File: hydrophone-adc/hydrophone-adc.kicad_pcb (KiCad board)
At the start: 4 copper layers, 152.8 x 66.3 mm, 202 parts, among them J1001 TEST_1P, J1002 TEST_1P, J1003 TEST_1P, J1004 TEST_1P, J1005 TEST_1P, J1006 TEST_1P, J1007 TEST_1P, J1101 TEST_1P, J1102 TEST_1P, J1201 TEST_1P, J1202 TEST_1P, J1203 TEST_1P, J1204 TEST_1P, J1205 TEST_1P, J1206 TEST_1P, J1207 TEST_1P, J1301 BARREL_JACK, J401 CONN_COAXIAL, J402 CONN_COAXIAL, J403 CONN_COAXIAL, J404 CONN_COAXIAL, J501 TEST_1P, J502 TEST_1P, J601 TEST_1P, J602 TEST_1P, J603 TEST_1P, J604 TEST_1P, J605 TEST_1P, J606 TEST_1P, J607 TEST_1P, J701 TEST_1P, J702 TEST_1P, J801 TEST_1P, J802 TEST_1P, J803 TEST_1P, J804 TEST_1P, J805 TEST_1P, J806 TEST_1P, J807 TEST_1P, J901 TEST_1P, J902 TEST_1P, U1001 LM324, U1101 el5170, U1201 LM324, U1301 TS30013, U1302 LM2776, U1303 LT1963, U201 micro-zed-jx1, U301 micro-zed-jx2, U401 LTC2171-14, U501 el5170, U601 LM324, U701 el5170, U801 LM324, U901 el5170

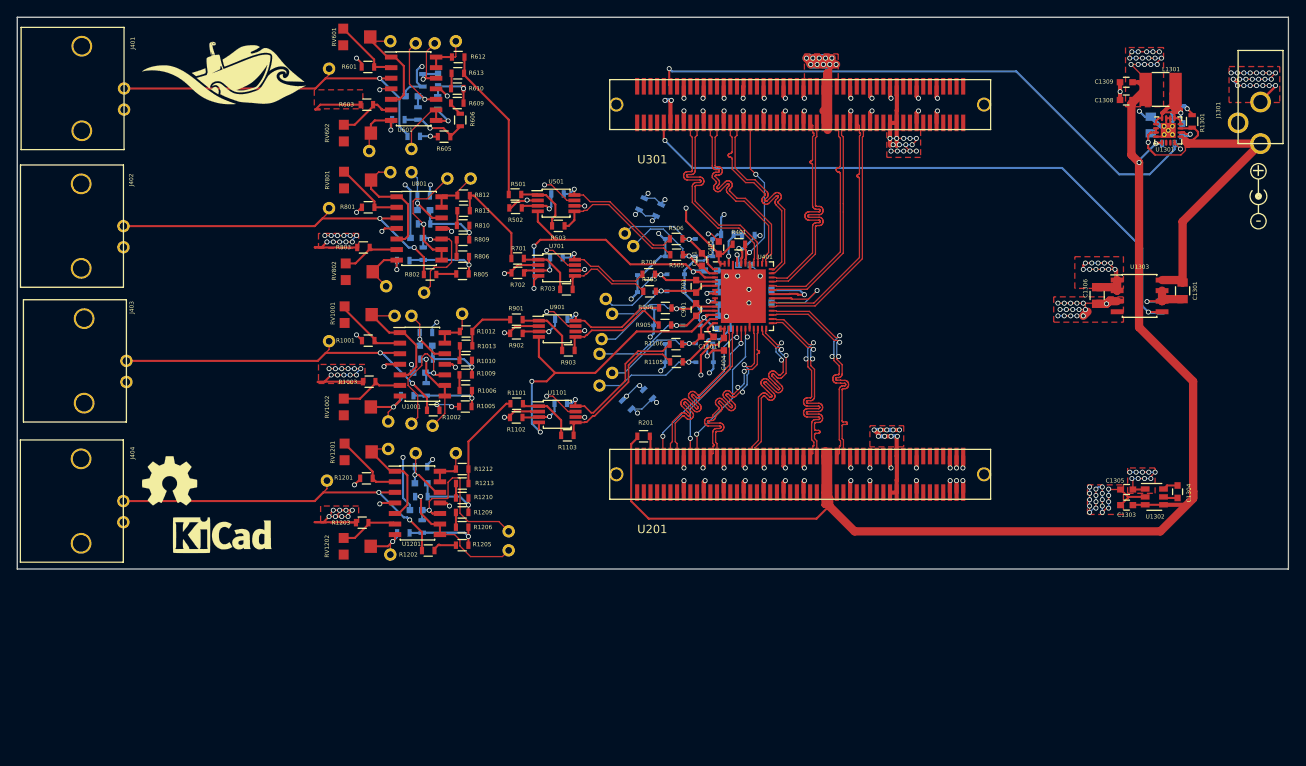
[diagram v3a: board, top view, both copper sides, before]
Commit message: Updated hydrophone board post review
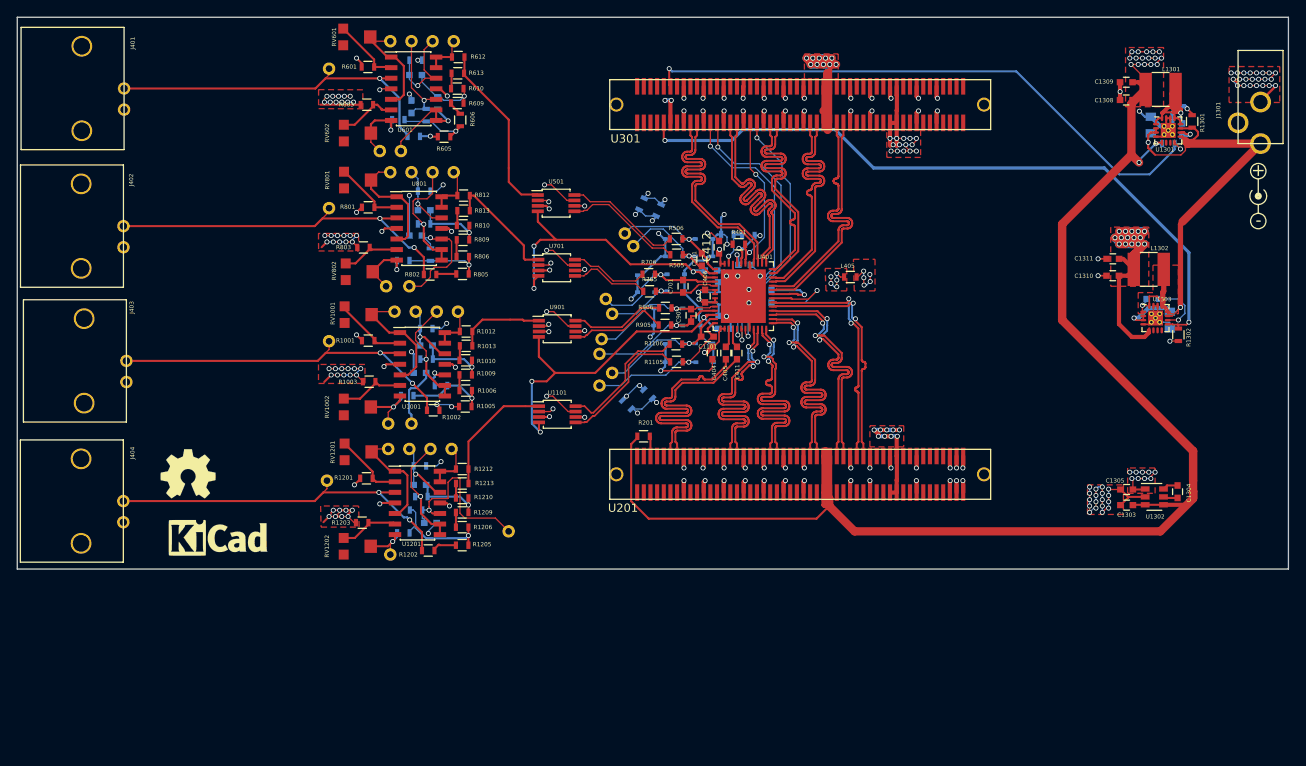
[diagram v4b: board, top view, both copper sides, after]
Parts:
- removed G***: LOGO, robosub_footprints:robosub_logo-large
- removed R1101, R1102, R1103, R1104, R501, R502, R503, R504, R701, R702, R703, R704, R901, R902, R903, R904: 10k .1%, Resistors_SMD:R_0603
- added C1310: 22u, Capacitors_SMD:C_0603, F.Cu at (215.4, 71.4)
- added C1311: 22u, Capacitors_SMD:C_0603, F.Cu at (215.4, 69.3)
- added C411: 100n, Capacitors_SMD:C_0603, F.Cu at (170.2, 80.7)
- added C412: 1u, Capacitors_SMD:C_0603, F.Cu at (168.1, 67.9)
- added L1302: 4.7u, robosub_footprints:Inductor-3.6mm-Pitch-4.0mm-Length-1.5mm-Width, F.Cu at (219.7, 70.6)
- added L405: Ferrite_Bead, Resistors_SMD:R_0603, F.Cu at (183.8, 71.5)
- C1301: moved to B.Cu
- C1306: value 10u -> 22n; footprint Capacitors_SMD:C_0805 -> Capacitors_SMD:C_0603; moved to B.Cu
- C406: moved to F.Cu
- R1302: value 100k -> 10k; moved to F.Cu
- U1303: value LT1963 -> TS30042; footprint Housings_SOIC:SOIC-8_3.9x4.9mm_Pitch1.27mm -> Housings_DFN_QFN:QFN-16-1EP_3x3mm_Pitch0.5mm_ThermalVias
- moved J1205 15.4 mm to (133.3, 92.2)
- moved J1005 13.7 mm to (134.1, 75.7)
- moved C405 12.7 mm to (168.9, 80.7)
- moved R807 7.51 mm to (132.6, 61.2), turned to 0 degrees
- moved R1007 7.32 mm to (132.8, 77.7), turned to 0 degrees
- moved R1207 7.29 mm to (132.1, 94.2), turned to 0 degrees
- moved R811 7.10 mm to (133.3, 68.8), turned to 270 degrees
- moved C1306 6.73 mm to (220.2, 74.2), turned to 0 degrees
- moved R1011 6.64 mm to (134.6, 84.6)
- moved R607 6.40 mm to (131.6, 45.5), turned to 0 degrees
- moved R1211 5.25 mm to (131.6, 99.5), turned to 180 degrees
- moved C1202 4.89 mm to (133.3, 101.1), turned to 180 degrees
- moved C602 4.52 mm to (131.1, 51.1)
- moved R611 4.20 mm to (132.8, 52.1)
- moved R1302 4.00 mm to (223.3, 78.5), turned to 270 degrees
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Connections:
- C1001 pad 2: GNDREF -> Net-(C1001-Pad2)
- C1002 pad 1: Net-(C1002-Pad1) -> GNDREF
- C1201 pad 2: GNDREF -> Net-(C1201-Pad2)
- C1202 pad 1: Net-(C1202-Pad1) -> GNDREF
- C1306 pad 1: +1V8 -> Net-(C1306-Pad1)
- C1306 pad 2: GND -> Net-(C1306-Pad2)
- C404 pad 1: +1V8 -> /ADC/1v8_analog
- C405 pad 1: +1V8 -> /samp_clk+
- C405 pad 2: GNDREF -> /ADC/enc+
- C601 pad 2: GNDREF -> Net-(C601-Pad2)
- C602 pad 1: Net-(C602-Pad1) -> GNDREF
- C801 pad 2: GNDREF -> Net-(C801-Pad2)
- C802 pad 1: Net-(C802-Pad1) -> GNDREF
- J1004 pad 1: Net-(C1001-Pad1) -> Net-(C1002-Pad2)
- J1006 pad 1: Net-(C1002-Pad1) -> Net-(C1001-Pad1)
- J1204 pad 1: Net-(C1201-Pad1) -> Net-(C1202-Pad2)
- J1206 pad 1: Net-(C1202-Pad1) -> Net-(C1201-Pad1)
- J604 pad 1: Net-(C601-Pad1) -> Net-(C602-Pad2)
- J606 pad 1: Net-(C602-Pad1) -> Net-(C601-Pad1)
- J804 pad 1: Net-(C801-Pad1) -> Net-(C802-Pad2)
- J806 pad 1: Net-(C802-Pad1) -> Net-(C801-Pad1)
- R1007 pad 1: Net-(R1004-Pad1) -> Net-(C1001-Pad1)
- R1007 pad 2: Net-(C1001-Pad1) -> GNDREF
- R1008 pad 1: Net-(C1002-Pad2) -> Net-(C1001-Pad2)
- R1009 pad 1: Net-(C1002-Pad2) -> Net-(C1001-Pad2)
- R1010 pad 1: Net-(C1002-Pad2) -> Net-(C1001-Pad2)
- R1011 pad 1: Net-(C1002-Pad1) -> Net-(C1002-Pad2)
- R1011 pad 2: GNDREF -> Net-(R1004-Pad1)
- R1105 pad 1: /ADC/Diff Conv4/v+ -> /ADC/Diff Conv4/v-
- R1106 pad 1: /ADC/Diff Conv4/v- -> /ADC/Diff Conv4/v+
- R1207 pad 1: Net-(R1204-Pad1) -> Net-(C1201-Pad1)
- R1207 pad 2: Net-(C1201-Pad1) -> GNDREF
- R1208 pad 1: Net-(C1202-Pad2) -> Net-(C1201-Pad2)
- R1209 pad 1: Net-(C1202-Pad2) -> Net-(C1201-Pad2)
- R1210 pad 1: Net-(C1202-Pad2) -> Net-(C1201-Pad2)
- R1211 pad 1: Net-(C1202-Pad1) -> Net-(C1202-Pad2)
- R1211 pad 2: GNDREF -> Net-(R1204-Pad1)
- R505 pad 1: /ADC/Diff Conv1/v+ -> /ADC/Diff Conv1/v-
- R506 pad 1: /ADC/Diff Conv1/v- -> /ADC/Diff Conv1/v+
- R607 pad 1: Net-(R604-Pad1) -> Net-(C601-Pad1)
- R607 pad 2: Net-(C601-Pad1) -> GNDREF
- R608 pad 1: Net-(C602-Pad2) -> Net-(C601-Pad2)
- R609 pad 1: Net-(C602-Pad2) -> Net-(C601-Pad2)
- R610 pad 1: Net-(C602-Pad2) -> Net-(C601-Pad2)
- R611 pad 1: Net-(C602-Pad1) -> Net-(C602-Pad2)
- R611 pad 2: GNDREF -> Net-(R604-Pad1)
- R705 pad 1: /ADC/Diff Conv2/v+ -> /ADC/Diff Conv2/v-
- R706 pad 1: /ADC/Diff Conv2/v- -> /ADC/Diff Conv2/v+
- R807 pad 1: Net-(R804-Pad1) -> Net-(C801-Pad1)
- R807 pad 2: Net-(C801-Pad1) -> GNDREF
- R808 pad 1: Net-(C802-Pad2) -> Net-(C801-Pad2)
- R809 pad 1: Net-(C802-Pad2) -> Net-(C801-Pad2)
- R810 pad 1: Net-(C802-Pad2) -> Net-(C801-Pad2)
- R811 pad 1: Net-(C802-Pad1) -> Net-(C802-Pad2)
- R811 pad 2: GNDREF -> Net-(R804-Pad1)
- R905 pad 1: /ADC/Diff Conv3/v+ -> /ADC/Diff Conv3/v-
- R906 pad 1: /ADC/Diff Conv3/v- -> /ADC/Diff Conv3/v+
- U1001 pad 10: Net-(C1001-Pad1) -> Net-(C1002-Pad2)
- U1001 pad 12: Net-(C1002-Pad1) -> Net-(C1001-Pad1)
- U1101 pad 1: Net-(R1101-Pad1) -> /ADC/Diff Conv4/Vin
- U1101 pad 3: Net-(R1102-Pad1) -> GNDREF
- U1101 pad 5: /ADC/Diff Conv4/v+ -> /ADC/Diff Conv4/v-
- U1101 pad 8: /ADC/Diff Conv4/v- -> /ADC/Diff Conv4/v+
- U1201 pad 10: Net-(C1201-Pad1) -> Net-(C1202-Pad2)
- U1201 pad 12: Net-(C1202-Pad1) -> Net-(C1201-Pad1)
- U1303 pad 1: +1V8 -> Net-(C1306-Pad1)
- U1303 pad 2: +1V8 -> /Power/Vin
- U1303 pad 3: GND -> /Power/Vin
- U1303 pad 4: (no net) -> GND
- U1303 pad 5: /vccio_en -> +1V8
- U1303 pad 6: GND -> (no net)
- U1303 pad 7: GND -> (no net)
- U1303 pad 8: /Power/Vin -> Net-(U1303-Pad8)
- U201 pad 10: /MicroZed-JX1/SE1 -> /MicroZed-JX1/SE0
- U201 pad 17: /SCK -> /MicroZed-JX1/LVDS2+
- U201 pad 19: /MOSI -> /MicroZed-JX1/LVDS2-
- U201 pad 23: /out4b+ -> /MicroZed-JX1/LVDS4+
- U201 pad 25: /out4b- -> /MicroZed-JX1/LVDS4-
- U201 pad 29: /MicroZed-JX1/LVDS6+ -> /out4b+
- U201 pad 31: /MicroZed-JX1/LVDS6- -> /out4b-
- U201 pad 35: /out4a+ -> /MicroZed-JX1/LVDS8+
- U201 pad 37: /out4a- -> /MicroZed-JX1/LVDS8-
- U201 pad 41: /MicroZed-JX1/LVDS10+ -> /out4a+
- U201 pad 43: /MicroZed-JX1/LVDS10- -> /out4a-
- U201 pad 67: /MicroZed-JX1/LVDS18+ -> /fr_clk+
- U201 pad 69: /MicroZed-JX1/LVDS18- -> /fr_clk-
- U201 pad 9: /~CS -> /MicroZed-JX1/SE1
- U301 pad 24: /out1b+ -> /~CS
- U301 pad 26: /out1b- -> /SCK
- U301 pad 30: /out2a+ -> /out1b+
- U301 pad 32: /out2a- -> /out1b-
- U301 pad 38: /MicroZed-JX2/LVDS7- -> /MOSI
- U301 pad 42: /MicroZed-JX2/LVDS9+ -> /out2a+
- U301 pad 44: /MicroZed-JX2/LVDS9- -> /out2a-
- U301 pad 68: /fr_clk+ -> /MicroZed-JX2/LVDS17+
- U301 pad 70: /fr_clk- -> /MicroZed-JX2/LVDS17-
- U401 pad 15: +1V8 -> /ADC/1v8_analog
- U401 pad 16: +1V8 -> /ADC/1v8_analog
- U401 pad 17: /samp_clk+ -> /ADC/enc+
- U401 pad 18: /samp_clk- -> /ADC/enc-
- U401 pad 51: +1V8 -> /ADC/1v8_analog
- U401 pad 52: +1V8 -> /ADC/1v8_analog
- U501 pad 1: Net-(R501-Pad1) -> /ADC/Diff Conv1/Vin
- U501 pad 3: Net-(R502-Pad1) -> GNDREF
- U501 pad 5: /ADC/Diff Conv1/v+ -> /ADC/Diff Conv1/v-
- U501 pad 8: /ADC/Diff Conv1/v- -> /ADC/Diff Conv1/v+
- U601 pad 10: Net-(C601-Pad1) -> Net-(C602-Pad2)
- U601 pad 12: Net-(C602-Pad1) -> Net-(C601-Pad1)
- U701 pad 1: Net-(R701-Pad1) -> /ADC/Diff Conv2/Vin
- U701 pad 3: Net-(R702-Pad1) -> GNDREF
- U701 pad 5: /ADC/Diff Conv2/v+ -> /ADC/Diff Conv2/v-
- U701 pad 8: /ADC/Diff Conv2/v- -> /ADC/Diff Conv2/v+
- U801 pad 10: Net-(C801-Pad1) -> Net-(C802-Pad2)
- U801 pad 12: Net-(C802-Pad1) -> Net-(C801-Pad1)
- U901 pad 1: Net-(R901-Pad1) -> /ADC/Diff Conv3/Vin
- U901 pad 3: Net-(R902-Pad1) -> GNDREF
- U901 pad 5: /ADC/Diff Conv3/v+ -> /ADC/Diff Conv3/v-
- U901 pad 8: /ADC/Diff Conv3/v- -> /ADC/Diff Conv3/v+
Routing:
- net /ADC/1v8_analog: track 0.00 -> 45.7 mm, vias 0 -> 7
- net /vccio_en: track 76.3 -> 96.9 mm
- net Net-(C1306-Pad1): track 0.00 -> 18.1 mm, vias 0 -> 1
- net /SCK: track 17.9 -> 34.4 mm
- net GND: track 190.0 -> 173.7 mm, vias 117 -> 103
- net /~CS: track 19.3 -> 33.0 mm
- net Net-(C1202-Pad2): track 8.67 -> 22.1 mm
- net Net-(C1201-Pad1): track 21.5 -> 8.55 mm
- net /MOSI: track 18.0 -> 30.4 mm
- net /Power/Vin: track 48.5 -> 59.2 mm, vias 1 -> 3
- net Net-(C602-Pad1): track 8.95 -> 0.00 mm, vias 1 -> 0
- net Net-(C601-Pad2): track 0.00 -> 8.93 mm, vias 0 -> 1
- net Net-(C1201-Pad2): track 0.00 -> 8.55 mm, vias 0 -> 1
- net Net-(C1202-Pad1): track 8.55 -> 0.00 mm, vias 1 -> 0
- net Net-(C1002-Pad1): track 8.54 -> 0.00 mm, vias 1 -> 0
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- added copper zone on F.Cu, net /ADC/1v8_analog
- added copper zone on F.Cu, net Net-(C1306-Pad1)
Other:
- net class Default: clearance 0.1524 -> 0.127
- rule trace_clearance: 0.1524 -> 0.127

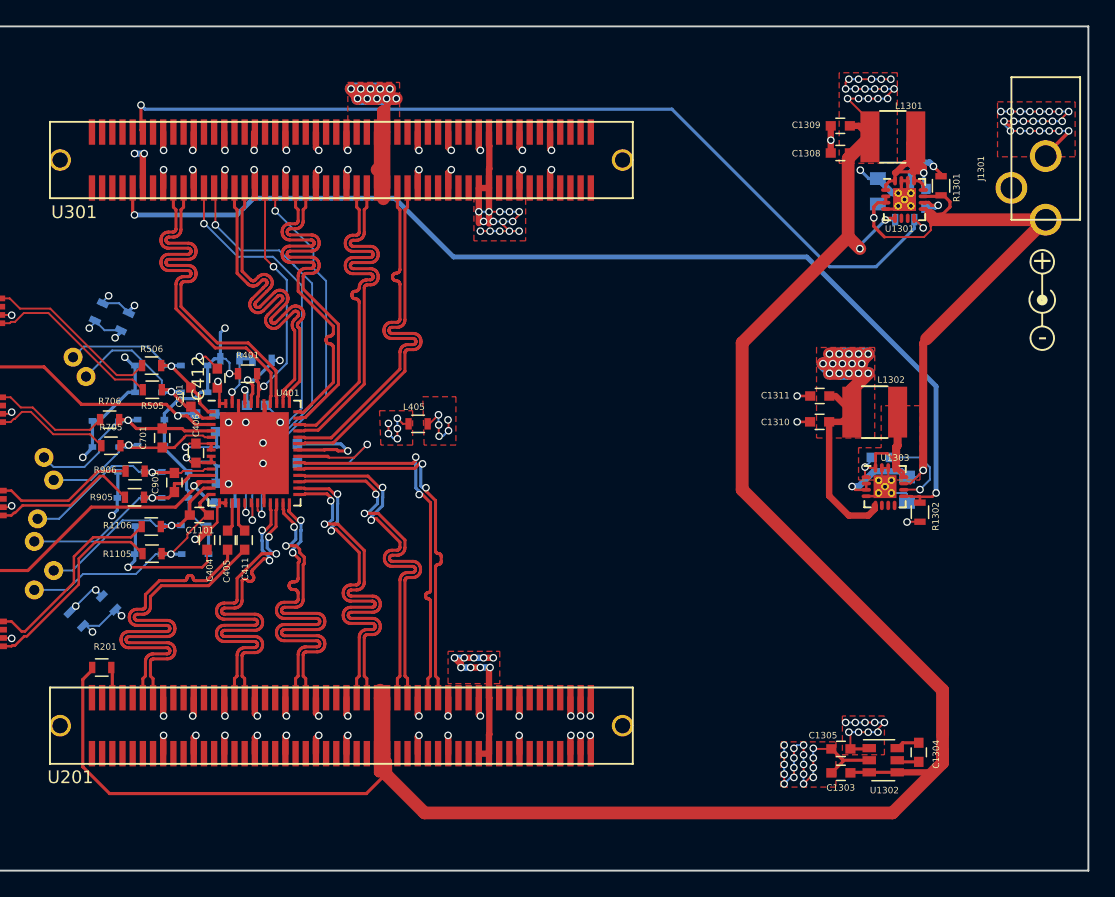
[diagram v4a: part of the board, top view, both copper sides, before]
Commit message: Added LEDs to board and schematic
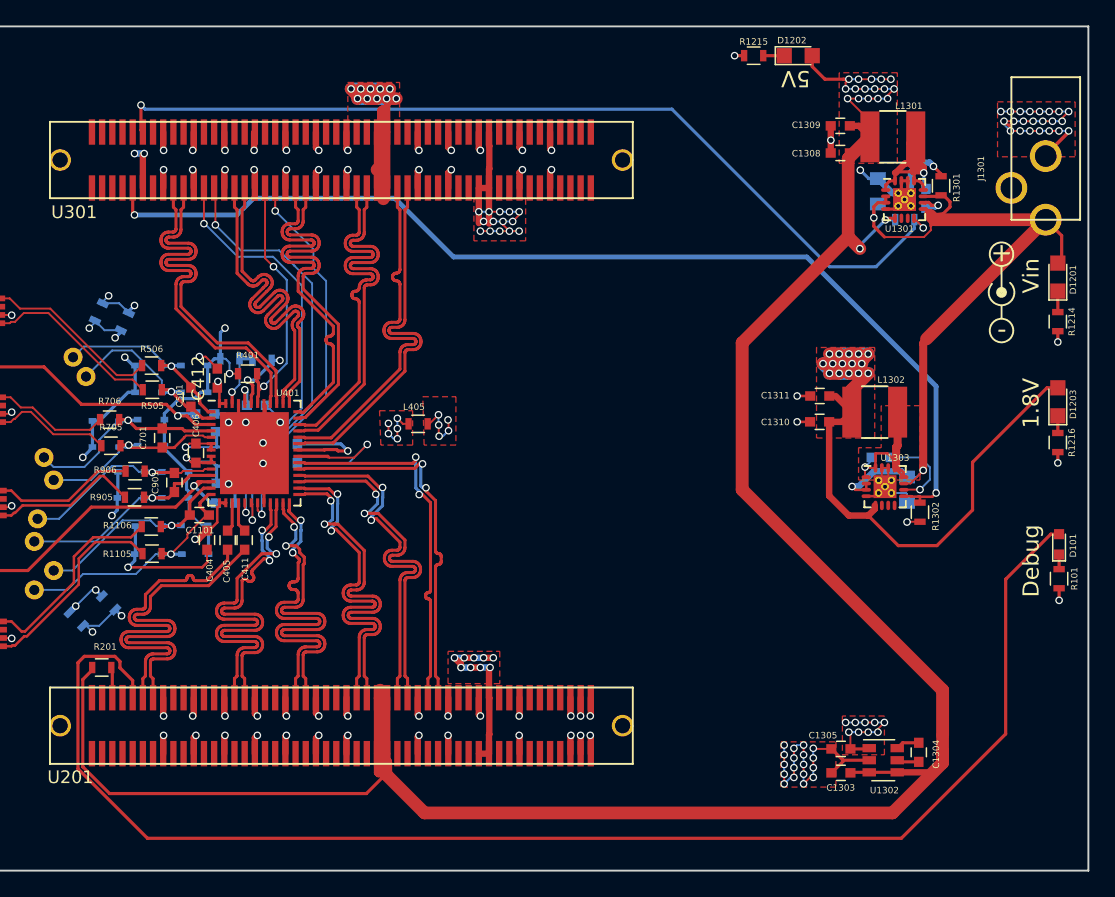
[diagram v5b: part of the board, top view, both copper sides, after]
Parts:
- added D101: ORG, LEDs:LED_0603, F.Cu at (234.2, 81.0)
- added D1201: YLW, LEDs:LED_0805, F.Cu at (234.1, 60.0)
- added D1202: RED, LEDs:LED_0805, F.Cu at (213.7, 42.6)
- added D1203: GRN, LEDs:LED_0805, F.Cu at (234.1, 69.8)
- added R101: 1k, Resistors_SMD:R_0603, F.Cu at (234.2, 83.7)
- added R1214: 1k, Resistors_SMD:R_0603, F.Cu at (234.1, 63.5)
- added R1215: 1k, Resistors_SMD:R_0603, F.Cu at (210.2, 42.6)
- added R1216: 1k, Resistors_SMD:R_0603, F.Cu at (234.1, 73.0)
- moved REF** 3.26 mm to (229.6, 61.2)
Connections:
- net /samp_clk+ renamed /enc+
- net /samp_clk- renamed /enc-
- R401 pad 2: /MISO -> /MOSI
- U201 pad 10: /MicroZed-JX1/SE0 -> /MicroZed-JX1/SE1
- U201 pad 9: /MicroZed-JX1/SE1 -> /MicroZed-JX1/SE0
- U301 pad 36: /MISO -> /MOSI
- U301 pad 38: /MOSI -> /MISO
- U401 pad 21: /MOSI -> /MISO
- U401 pad 46: /MISO -> /MOSI
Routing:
- net /MicroZed-JX1/SE0: track 0.00 -> 111.7 mm
- net +1V8: track 103.6 -> 126.8 mm
- net /MOSI: track 30.4 -> 20.1 mm
- net /MISO: track 20.1 -> 30.4 mm
- net +5V: track 242.1 -> 246.3 mm
- net /Power/Vin: track 59.2 -> 63.3 mm
- net GND: track 173.7 -> 177.1 mm, vias 103 -> 107
- net Net-(D1202-Pad1): track 0.00 -> 1.65 mm
- net Net-(D1201-Pad1): track 0.00 -> 1.65 mm
- net Net-(D1203-Pad1): track 0.00 -> 1.35 mm
- net Net-(D101-Pad1): track 0.00 -> 1.15 mm
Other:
- board text added: "1.8V"
- board text added: "5V"
- board text added: "Debug"
- board text added: "Vin"

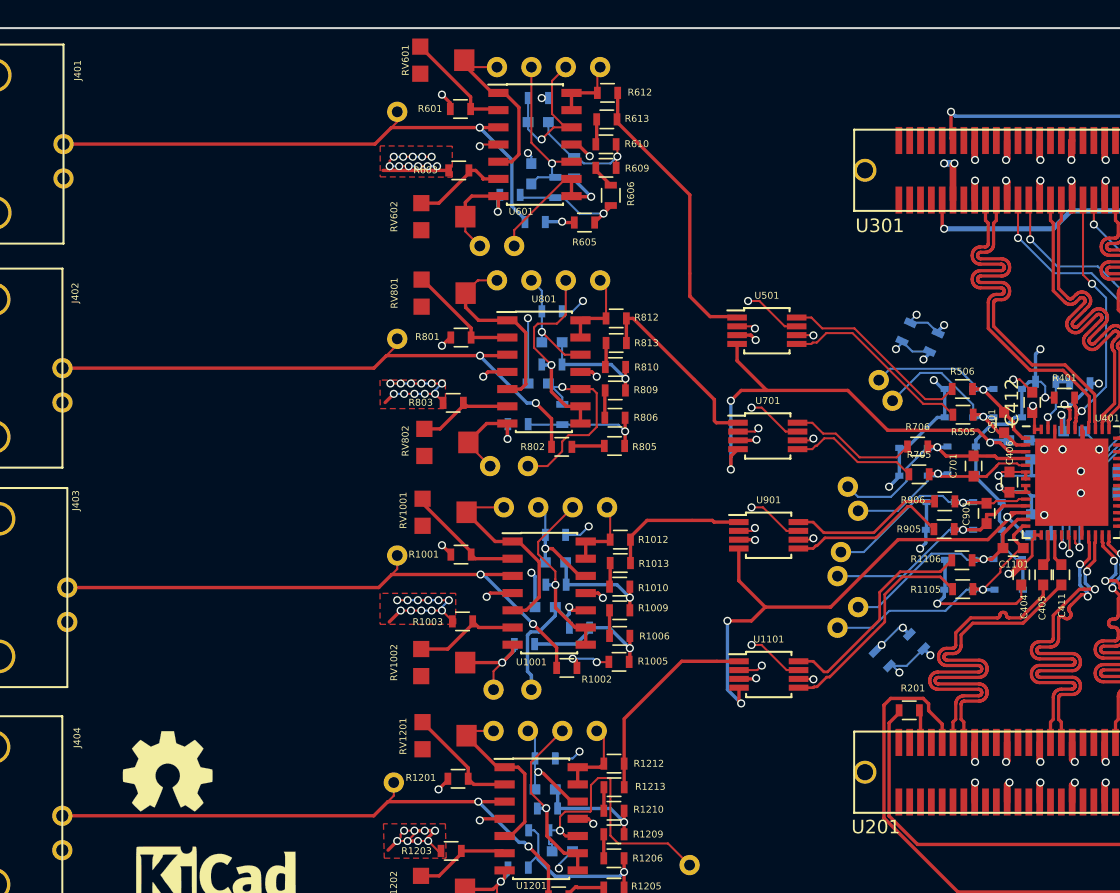
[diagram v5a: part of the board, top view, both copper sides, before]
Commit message: Added Robosub logo to hydrophone board
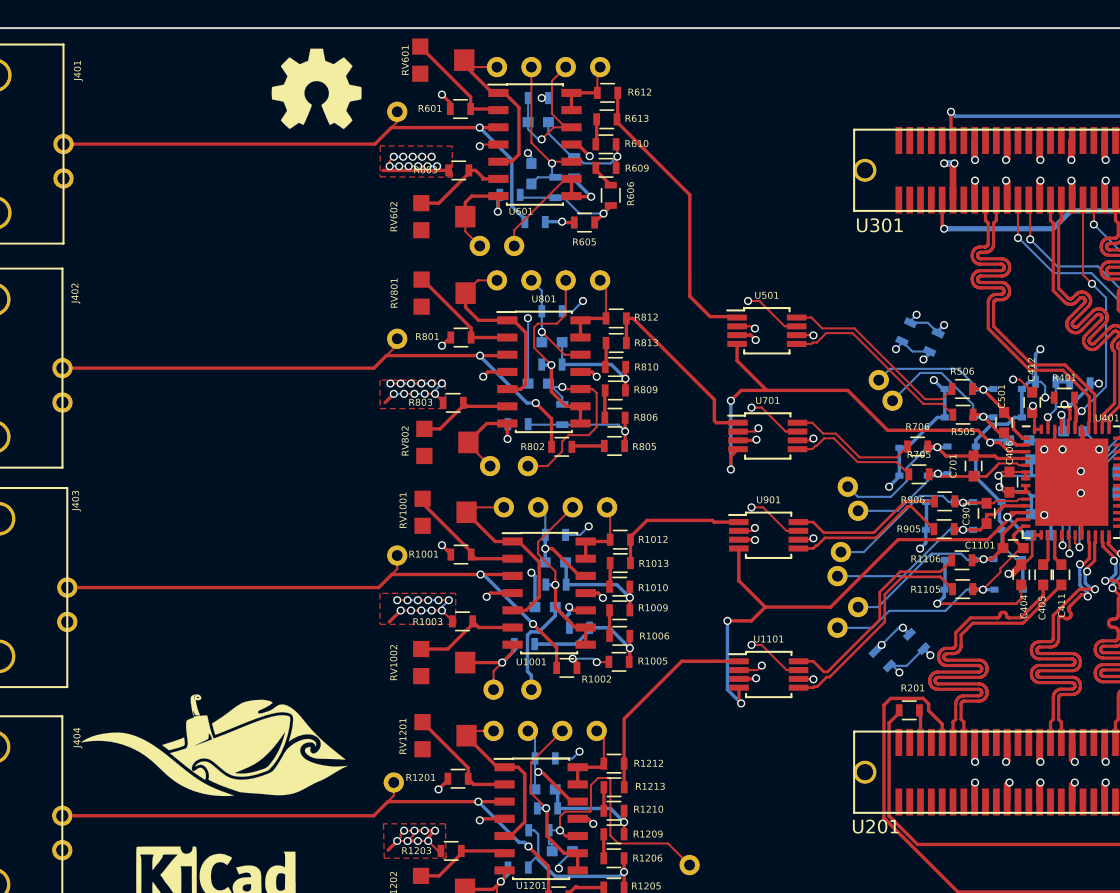
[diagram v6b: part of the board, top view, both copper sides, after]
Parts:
- added G***: LOGO, robosub_footprints:robosub_logo-large, F.Cu at (107.8, 93.5)
- moved REF*** 51.6 mm to (115.2, 44.8)
